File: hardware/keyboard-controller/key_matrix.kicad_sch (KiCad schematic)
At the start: 21 parts, among them J5 Keybed_Connector, SW4 OCTAVE_UP, SW5 OCTAVE_DOWN, U10 74HC164, U9 74HC164

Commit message: Added analog switch for analog input
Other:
- title: (none) -> Key Matrix
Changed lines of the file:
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@@
 (kicad_sch (version 20211123) (generator eeschema)
   (paper "A4")
+  (title_block
+    (title "Key Matrix")
+    (rev "1")
+  )
   (junction (at 215.9 50.8) (diameter 0) (color 0 0 0 0)
   )

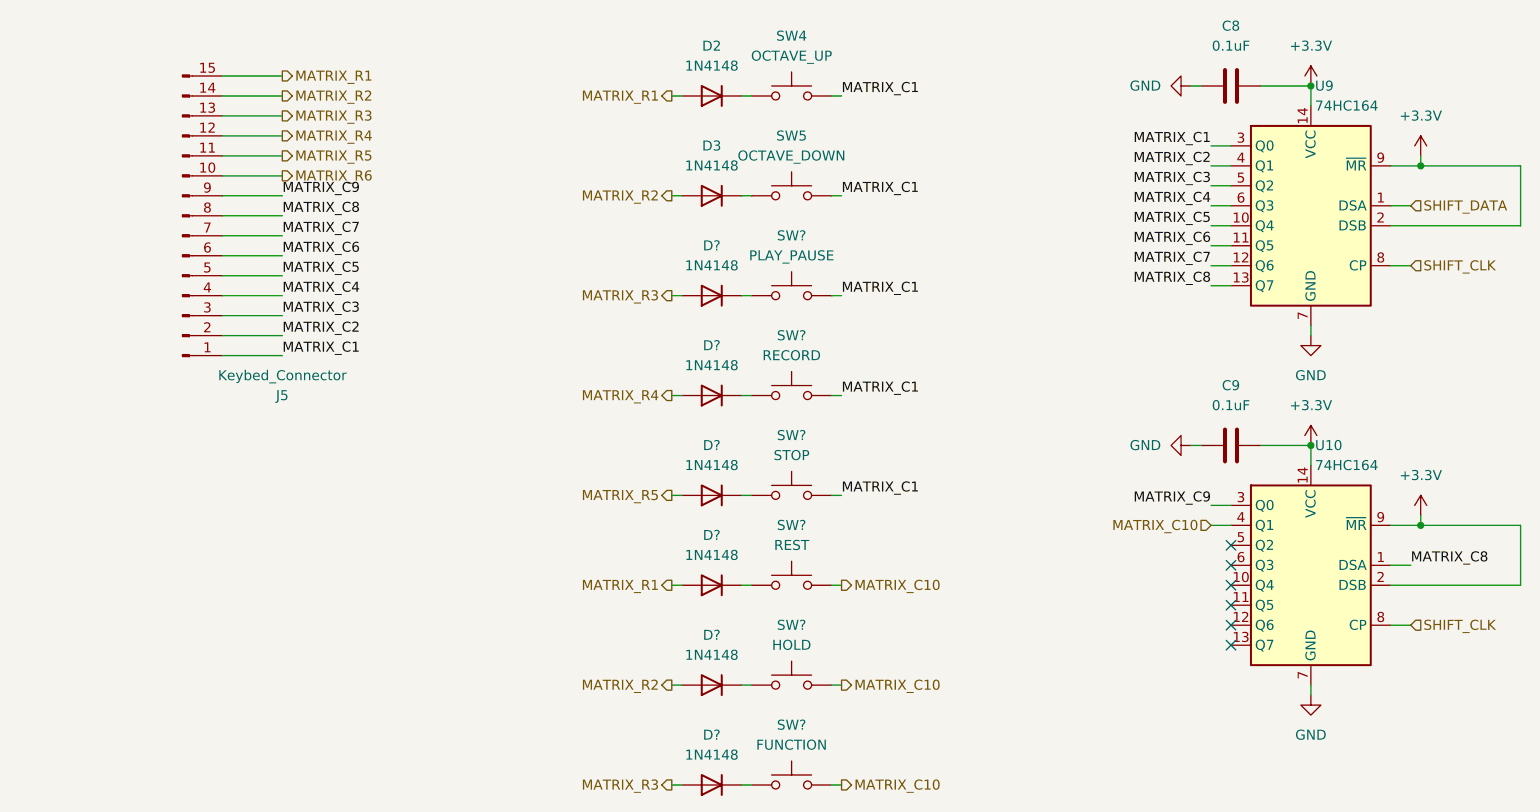
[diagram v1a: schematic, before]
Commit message: Added footprint for rotary switches
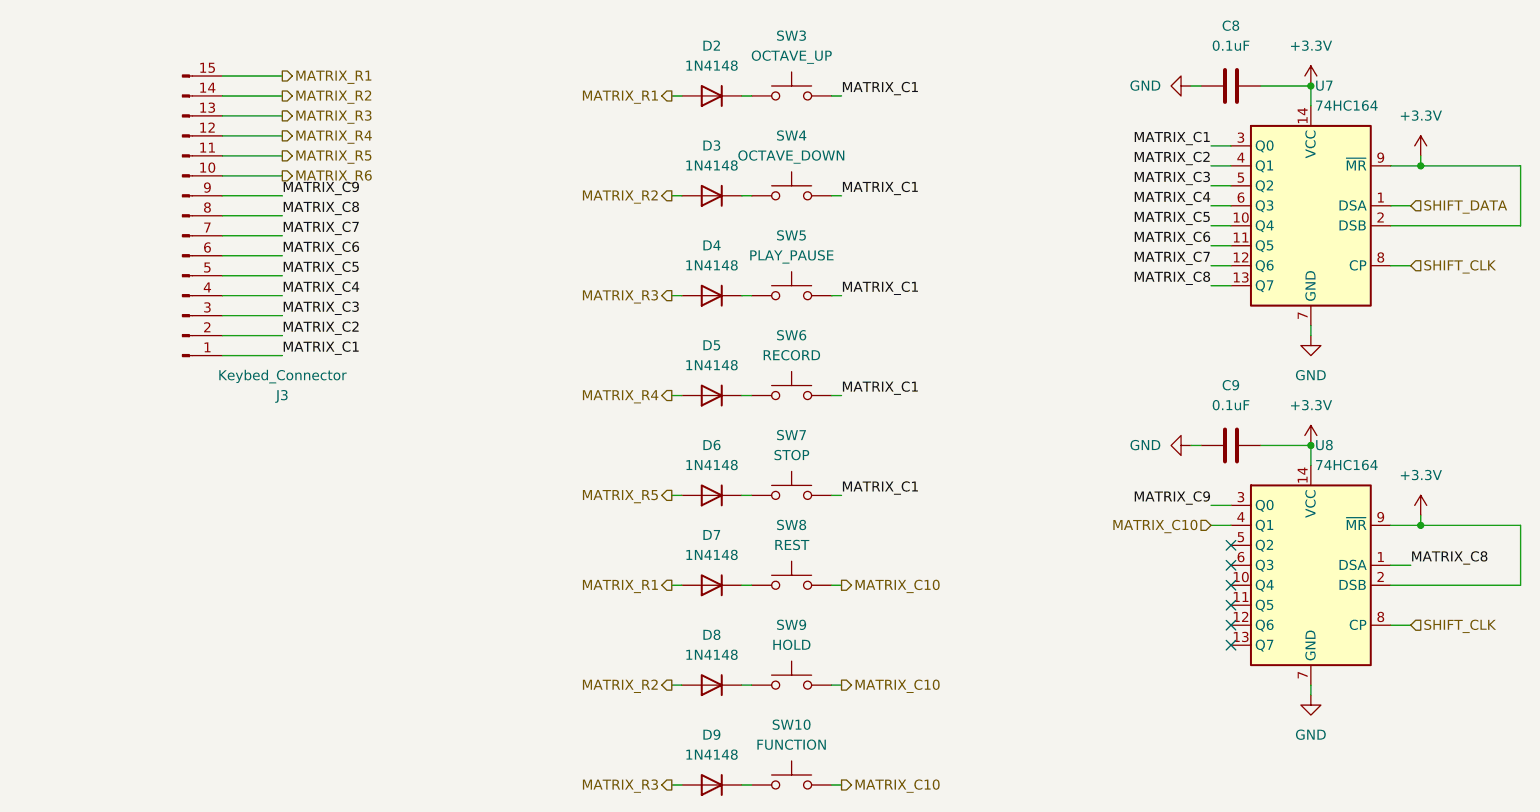
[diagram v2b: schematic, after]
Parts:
- gave numbers to parts that had none: 12
- renumbered J5 to J3, SW4 to SW3, SW5 to SW4, U9 to U7, U10 to U8
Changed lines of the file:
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@@
   (symbol (lib_id "Diode:1N4148") (at 139.7 127 180) (unit 1)
     (in_bom yes) (on_board yes) (fields_autoplaced)
-    (property "Reference" "D?" (id 0) (at 139.7 120.65 0))
+    (property "Reference" "D8" (id 0) (at 139.7 120.65 0))
     (property "Value" "1N4148" (id 1) (at 139.7 123.19 0))
     (property "Footprint" "Diode_THT:D_DO-35_SOD27_P7.62mm_Horizontal" (id 2) (at 139.7 122.555 0)
@@
   (symbol (lib_id "Diode:1N4148") (at 139.7 90.17 180) (unit 1)
     (in_bom yes) (on_board yes) (fields_autoplaced)
-    (property "Reference" "D?" (id 0) (at 139.7 83.82 0))
+    (property "Reference" "D5" (id 0) (at 139.7 83.82 0))
     (property "Value" "1N4148" (id 1) (at 139.7 86.36 0))
     (property "Footprint" "Diode_THT:D_DO-35_SOD27_P7.62mm_Horizontal" (id 2) (at 139.7 85.725 0)
@@
   (symbol (lib_id "Switch:SW_Push") (at 149.86 52.07 0) (unit 1)
     (in_bom yes) (on_board yes) (fields_autoplaced)
-    (property "Reference" "SW4" (id 0) (at 149.86 44.45 0))
+    (property "Reference" "SW3" (id 0) (at 149.86 44.45 0))
     (property "Value" "OCTAVE_UP" (id 1) (at 149.86 46.99 0))
     (property "Footprint" "" (id 2) (at 149.86 46.99 0)
@@
   (symbol (lib_id "Switch:SW_Push") (at 149.86 90.17 0) (unit 1)
     (in_bom yes) (on_board yes) (fields_autoplaced)
-    (property "Reference" "SW?" (id 0) (at 149.86 82.55 0))
+    (property "Reference" "SW6" (id 0) (at 149.86 82.55 0))
     (property "Value" "RECORD" (id 1) (at 149.86 85.09 0))
     (property "Footprint" "" (id 2) (at 149.86 85.09 0)
@@
   (symbol (lib_id "Connector:Conn_01x15_Male") (at 72.39 67.31 0) (mirror x) (unit 1)
     (in_bom yes) (on_board yes)
-    (property "Reference" "J5" (id 0) (at 85.09 90.17 0))
+    (property "Reference" "J3" (id 0) (at 85.09 90.17 0))
     (property "Value" "Keybed_Connector" (id 1) (at 85.09 87.63 0))
     (property "Footprint" "Connector_IDC:IDC-Header_2x08_P2.54mm_Vertical" (id 2) (at 72.39 67.31 0)
@@
   (symbol (lib_id "Switch:SW_Push") (at 149.86 64.77 0) (unit 1)
     (in_bom yes) (on_board yes) (fields_autoplaced)
-    (property "Reference" "SW5" (id 0) (at 149.86 57.15 0))
+    (property "Reference" "SW4" (id 0) (at 149.86 57.15 0))
     (property "Value" "OCTAVE_DOWN" (id 1) (at 149.86 59.69 0))
     (property "Footprint" "" (id 2) (at 149.86 59.69 0)
@@
   (symbol (lib_id "Diode:1N4148") (at 139.7 102.87 180) (unit 1)
     (in_bom yes) (on_board yes) (fields_autoplaced)
-    (property "Reference" "D?" (id 0) (at 139.7 96.52 0))
+    (property "Reference" "D6" (id 0) (at 139.7 96.52 0))
     (property "Value" "1N4148" (id 1) (at 139.7 99.06 0))
     (property "Footprint" "Diode_THT:D_DO-35_SOD27_P7.62mm_Horizontal" (id 2) (at 139.7 98.425 0)
@@
   (symbol (lib_id "power:GND") (at 215.9 82.55 0) (unit 1)
     (in_bom yes) (on_board yes) (fields_autoplaced)
-    (property "Reference" "#PWR033" (id 0) (at 215.9 88.9 0)
+    (property "Reference" "#PWR034" (id 0) (at 215.9 88.9 0)
       (effects (font (size 1.27 1.27)) hide)
     )
@@
   (symbol (lib_id "Switch:SW_Push") (at 149.86 139.7 0) (unit 1)
     (in_bom yes) (on_board yes) (fields_autoplaced)
-    (property "Reference" "SW?" (id 0) (at 149.86 132.08 0))
+    (property "Reference" "SW10" (id 0) (at 149.86 132.08 0))
     (property "Value" "FUNCTION" (id 1) (at 149.86 134.62 0))
     (property "Footprint" "" (id 2) (at 149.86 134.62 0)
@@
   (symbol (lib_id "Switch:SW_Push") (at 149.86 77.47 0) (unit 1)
     (in_bom yes) (on_board yes) (fields_autoplaced)
-    (property "Reference" "SW?" (id 0) (at 149.86 69.85 0))
+    (property "Reference" "SW5" (id 0) (at 149.86 69.85 0))
     (property "Value" "PLAY_PAUSE" (id 1) (at 149.86 72.39 0))
     (property "Footprint" "" (id 2) (at 149.86 72.39 0)
@@
   (symbol (lib_id "power:GND") (at 200.66 50.8 270) (unit 1)
     (in_bom yes) (on_board yes) (fields_autoplaced)
-    (property "Reference" "#PWR030" (id 0) (at 194.31 50.8 0)
+    (property "Reference" "#PWR031" (id 0) (at 194.31 50.8 0)
       (effects (font (size 1.27 1.27)) hide)
     )
@@
   (symbol (lib_id "Diode:1N4148") (at 139.7 139.7 180) (unit 1)
     (in_bom yes) (on_board yes) (fields_autoplaced)
-    (property "Reference" "D?" (id 0) (at 139.7 133.35 0))
+    (property "Reference" "D9" (id 0) (at 139.7 133.35 0))
     (property "Value" "1N4148" (id 1) (at 139.7 135.89 0))
     (property "Footprint" "Diode_THT:D_DO-35_SOD27_P7.62mm_Horizontal" (id 2) (at 139.7 135.255 0)
@@
   (symbol (lib_id "power:+3.3V") (at 229.87 105.41 0) (unit 1)
     (in_bom yes) (on_board yes) (fields_autoplaced)
-    (property "Reference" "#PWR037" (id 0) (at 229.87 109.22 0)
+    (property "Reference" "#PWR038" (id 0) (at 229.87 109.22 0)
       (effects (font (size 1.27 1.27)) hide)
     )
@@
   (symbol (lib_id "Diode:1N4148") (at 139.7 114.3 180) (unit 1)
     (in_bom yes) (on_board yes) (fields_autoplaced)
-    (property "Reference" "D?" (id 0) (at 139.7 107.95 0))
+    (property "Reference" "D7" (id 0) (at 139.7 107.95 0))
     (property "Value" "1N4148" (id 1) (at 139.7 110.49 0))
     (property "Footprint" "Diode_THT:D_DO-35_SOD27_P7.62mm_Horizontal" (id 2) (at 139.7 109.855 0)
@@
   (symbol (lib_id "74xx:74HC164") (at 215.9 111.76 0) (mirror y) (unit 1)
     (in_bom yes) (on_board yes) (fields_autoplaced)
-    (property "Reference" "U10" (id 0) (at 216.4206 96.52 0)
+    (property "Reference" "U8" (id 0) (at 216.4206 96.52 0)
       (effects (font (size 1.27 1.27)) (justify right))
     )
@@
   (symbol (lib_id "Switch:SW_Push") (at 149.86 114.3 0) (unit 1)
     (in_bom yes) (on_board yes) (fields_autoplaced)
-    (property "Reference" "SW?" (id 0) (at 149.86 106.68 0))
+    (property "Reference" "SW8" (id 0) (at 149.86 106.68 0))
     (property "Value" "REST" (id 1) (at 149.86 109.22 0))
     (property "Footprint" "" (id 2) (at 149.86 109.22 0)
@@
   (symbol (lib_id "74xx:74HC164") (at 215.9 66.04 0) (mirror y) (unit 1)
     (in_bom yes) (on_board yes) (fields_autoplaced)
-    (property "Reference" "U9" (id 0) (at 216.4206 50.8 0)
+    (property "Reference" "U7" (id 0) (at 216.4206 50.8 0)
       (effects (font (size 1.27 1.27)) (justify right))
     )
@@
   (symbol (lib_id "Switch:SW_Push") (at 149.86 127 0) (unit 1)
     (in_bom yes) (on_board yes) (fields_autoplaced)
-    (property "Reference" "SW?" (id 0) (at 149.86 119.38 0))
+    (property "Reference" "SW9" (id 0) (at 149.86 119.38 0))
     (property "Value" "HOLD" (id 1) (at 149.86 121.92 0))
     (property "Footprint" "" (id 2) (at 149.86 121.92 0)
@@
   (symbol (lib_id "power:GND") (at 200.66 96.52 270) (unit 1)
     (in_bom yes) (on_board yes) (fields_autoplaced)
-    (property "Reference" "#PWR031" (id 0) (at 194.31 96.52 0)
+    (property "Reference" "#PWR032" (id 0) (at 194.31 96.52 0)
       (effects (font (size 1.27 1.27)) hide)
     )
@@
   (symbol (lib_id "Switch:SW_Push") (at 149.86 102.87 0) (unit 1)
     (in_bom yes) (on_board yes) (fields_autoplaced)
-    (property "Reference" "SW?" (id 0) (at 149.86 95.25 0))
+    (property "Reference" "SW7" (id 0) (at 149.86 95.25 0))
     (property "Value" "STOP" (id 1) (at 149.86 97.79 0))
     (property "Footprint" "" (id 2) (at 149.86 97.79 0)
@@
   (symbol (lib_id "Diode:1N4148") (at 139.7 77.47 180) (unit 1)
     (in_bom yes) (on_board yes) (fields_autoplaced)
-    (property "Reference" "D?" (id 0) (at 139.7 71.12 0))
+    (property "Reference" "D4" (id 0) (at 139.7 71.12 0))
     (property "Value" "1N4148" (id 1) (at 139.7 73.66 0))
     (property "Footprint" "Diode_THT:D_DO-35_SOD27_P7.62mm_Horizontal" (id 2) (at 139.7 73.025 0)
@@
   (symbol (lib_id "power:+3.3V") (at 215.9 96.52 0) (unit 1)
     (in_bom yes) (on_board yes) (fields_autoplaced)
-    (property "Reference" "#PWR034" (id 0) (at 215.9 100.33 0)
+    (property "Reference" "#PWR035" (id 0) (at 215.9 100.33 0)
       (effects (font (size 1.27 1.27)) hide)
     )
@@
   (symbol (lib_id "power:+3.3V") (at 229.87 59.69 0) (unit 1)
     (in_bom yes) (on_board yes) (fields_autoplaced)
-    (property "Reference" "#PWR036" (id 0) (at 229.87 63.5 0)
+    (property "Reference" "#PWR037" (id 0) (at 229.87 63.5 0)
       (effects (font (size 1.27 1.27)) hide)
     )
@@
   (symbol (lib_id "power:+3.3V") (at 215.9 50.8 0) (unit 1)
     (in_bom yes) (on_board yes) (fields_autoplaced)
-    (property "Reference" "#PWR032" (id 0) (at 215.9 54.61 0)
+    (property "Reference" "#PWR033" (id 0) (at 215.9 54.61 0)
       (effects (font (size 1.27 1.27)) hide)
     )
@@
   (symbol (lib_id "power:GND") (at 215.9 128.27 0) (unit 1)
     (in_bom yes) (on_board yes) (fields_autoplaced)
-    (property "Reference" "#PWR035" (id 0) (at 215.9 134.62 0)
-      (effects (font (size 1.27 1.27)) hide)
-    )
+    (property "Reference" "#PWR036" (id 0) (at 215.9 134.62 0)
+      (effects (font (size 1.27 1.27)) hide)
+    )

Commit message: Updated hardware_config and fixed sync_cn
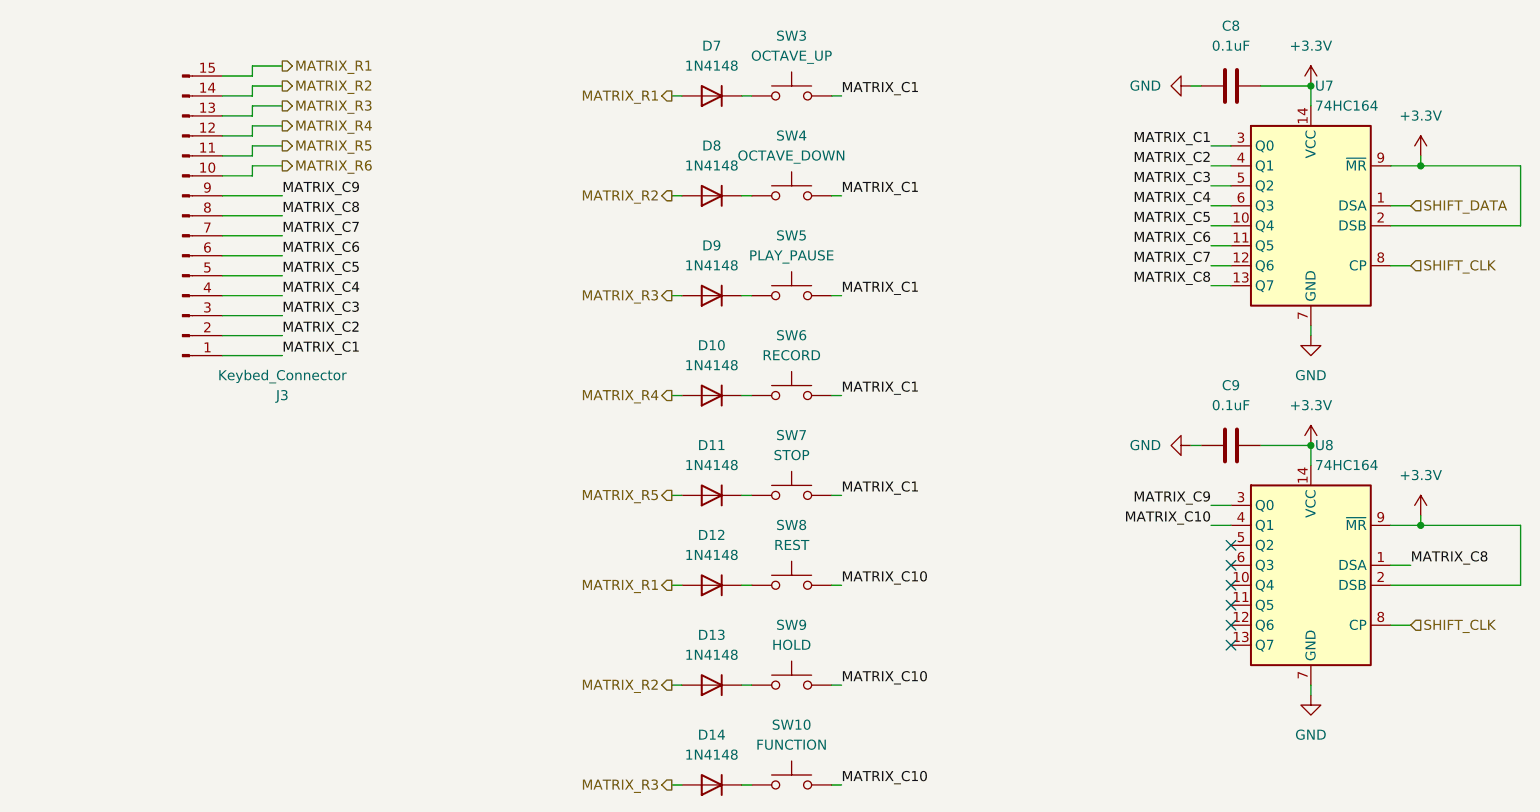
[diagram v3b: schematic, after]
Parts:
- C8, C9: Notes (none) -> Ceramic
- renumbered D5 to D10, D6 to D11, D7 to D12, D8 to D13, D9 to D14, D2 to D7, D3 to D8, D4 to D9

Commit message: Completed schematic rev1. Started placing pcb
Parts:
- removed J3: Keybed_Connector, Connector_IDC:IDC-Header_2x08_P2.54mm_Vertical, symbol Connector:Conn_01x15_Male
- added J3: Keybed Connector, Connector_IDC:IDC-Header_2x08_P2.54mm_Vertical, symbol Connector:Conn_01x16_Male
- SW10, SW3, SW4, SW5, SW6, SW7, SW8, SW9: footprint (none) -> Button_Switch_THT:SW_PUSH_6mm; Manufacturer (none) -> WEALTH METAL; Manufacturer Part No. (none) -> Tact Switch 6x6mm 5mm; Supplier Part No. (none) -> A-5127
- renumbered C8 to C7, C9 to C8, U7 to U6, U8 to U7
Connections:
- net MATRIX_C1: now also J3.1 (Pin_1)
- net MATRIX_C2: now also J3.2 (Pin_2)
- net MATRIX_C3: now also J3.3 (Pin_3)
- net MATRIX_C4: now also J3.4 (Pin_4)
- net MATRIX_C5: now also J3.5 (Pin_5)
- net MATRIX_C6: now also J3.6 (Pin_6)
- net MATRIX_C7: now also J3.7 (Pin_7)
- net MATRIX_C8: now also J3.8 (Pin_8)
- net MATRIX_C9: now also J3.9 (Pin_9)
- net MATRIX_R1: now also J3.15 (Pin_15)
- net MATRIX_R2: now also J3.14 (Pin_14)
- net MATRIX_R3: now also J3.13 (Pin_13)
- net MATRIX_R4: now also J3.12 (Pin_12)
- net MATRIX_R5: now also J3.11 (Pin_11)
- net MATRIX_R6: now also J3.10 (Pin_10)
- no-connect marks 6 -> 7

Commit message: Completed initial pcb design
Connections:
- net +3V3 renamed +3.3V

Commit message: Converted PCB to 2-layer
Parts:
- SW10: value FUNCTION -> REST
- SW6: value RECORD -> STOP
- SW7: value STOP -> RECORD
- SW8: value REST -> HOLD
- SW9: value HOLD -> FUNC
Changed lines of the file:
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@@
     (in_bom yes) (on_board yes) (fields_autoplaced)
     (property "Reference" "SW6" (id 0) (at 149.86 82.55 0))
-    (property "Value" "RECORD" (id 1) (at 149.86 85.09 0))
+    (property "Value" "STOP" (id 1) (at 149.86 85.09 0))
     (property "Footprint" "Button_Switch_THT:SW_PUSH_6mm" (id 2) (at 149.86 85.09 0)
       (effects (font (size 1.27 1.27)) hide)
@@
     (in_bom yes) (on_board yes) (fields_autoplaced)
     (property "Reference" "SW10" (id 0) (at 149.86 132.08 0))
-    (property "Value" "FUNCTION" (id 1) (at 149.86 134.62 0))
+    (property "Value" "REST" (id 1) (at 149.86 134.62 0))
     (property "Footprint" "Button_Switch_THT:SW_PUSH_6mm" (id 2) (at 149.86 134.62 0)
       (effects (font (size 1.27 1.27)) hide)
@@
     (in_bom yes) (on_board yes) (fields_autoplaced)
     (property "Reference" "SW8" (id 0) (at 149.86 106.68 0))
-    (property "Value" "REST" (id 1) (at 149.86 109.22 0))
+    (property "Value" "HOLD" (id 1) (at 149.86 109.22 0))
     (property "Footprint" "Button_Switch_THT:SW_PUSH_6mm" (id 2) (at 149.86 109.22 0)
       (effects (font (size 1.27 1.27)) hide)
@@
     (in_bom yes) (on_board yes) (fields_autoplaced)
     (property "Reference" "SW9" (id 0) (at 149.86 119.38 0))
-    (property "Value" "HOLD" (id 1) (at 149.86 121.92 0))
+    (property "Value" "FUNC" (id 1) (at 149.86 121.92 0))
     (property "Footprint" "Button_Switch_THT:SW_PUSH_6mm" (id 2) (at 149.86 121.92 0)
       (effects (font (size 1.27 1.27)) hide)
@@
     (in_bom yes) (on_board yes) (fields_autoplaced)
     (property "Reference" "SW7" (id 0) (at 149.86 95.25 0))
-    (property "Value" "STOP" (id 1) (at 149.86 97.79 0))
+    (property "Value" "RECORD" (id 1) (at 149.86 97.79 0))
     (property "Footprint" "Button_Switch_THT:SW_PUSH_6mm" (id 2) (at 149.86 97.79 0)
       (effects (font (size 1.27 1.27)) hide)
